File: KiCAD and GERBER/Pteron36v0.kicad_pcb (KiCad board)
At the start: 2 copper layers, 140.1 x 108.1 mm, 56 parts, among them J1 AudioJack4, J2 AudioJack4, J3 Conn_01x04, SW10 SW_PUSH, SW12 SW_PUSH, SW13 SW_PUSH, SW14 SW_PUSH, SW15 SW_PUSH, SW17 SW_PUSH, SW18 SW_PUSH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

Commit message: merge version 1.2.0 pcb into main
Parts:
- SW10, SW12, SW13, SW14, SW15, SW17, SW18, SW19, SW20, SW22, SW23, SW24, SW26, SW27, SW28, SW7, SW8, SW9: footprint Universal-Switch-Footprint:MX-ALPs-PG1350-FLIP -> Universal-Switch-Footprint:MX-ALPs-PG1350-FLIP-fix
- moved D10 12.7 mm to (114.8, 114.3), turned to 102.5 degrees
- moved D15 12.1 mm to (96.3, 123.1), turned to 115 degrees
- moved D20 11.1 mm to (80.8, 134.2), turned to 127.5 degrees
- moved D17 10.4 mm to (150.0, 52.3), turned to 90 degrees
- moved D12 10.3 mm to (170.1, 52.8), turned to 90 degrees
- moved D18 10.1 mm to (150.0, 69.0), turned to 90 degrees
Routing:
- net /Row3: track 193.1 -> 170.5 mm
- net Net-(D17-Pad2): track 20.6 -> 36.2 mm
- net /Col3: track 197.4 -> 182.6 mm, vias 3 -> 2
- net Net-(D15-Pad2): track 18.9 -> 33.3 mm
- net /Row1: track 227.9 -> 213.9 mm
- net Net-(D13-Pad2): track 21.7 -> 35.2 mm
- net Net-(D8-Pad2): track 17.6 -> 30.5 mm
- net Net-(D7-Pad2): track 20.4 -> 33.3 mm
- net Net-(D26-Pad2): track 17.4 -> 30.1 mm
- net Net-(D28-Pad2): track 21.9 -> 34.6 mm
- net Net-(D22-Pad2): track 22.8 -> 35.5 mm
- net Net-(D27-Pad2): track 23.9 -> 36.5 mm
- net /Row2: track 238.3 -> 225.8 mm, vias 4 -> 3
- net Net-(D9-Pad2): track 19.9 -> 32.1 mm
- net Net-(D18-Pad2): track 17.5 -> 29.8 mm
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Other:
- board text added: "Pteron36 V1.2.0"

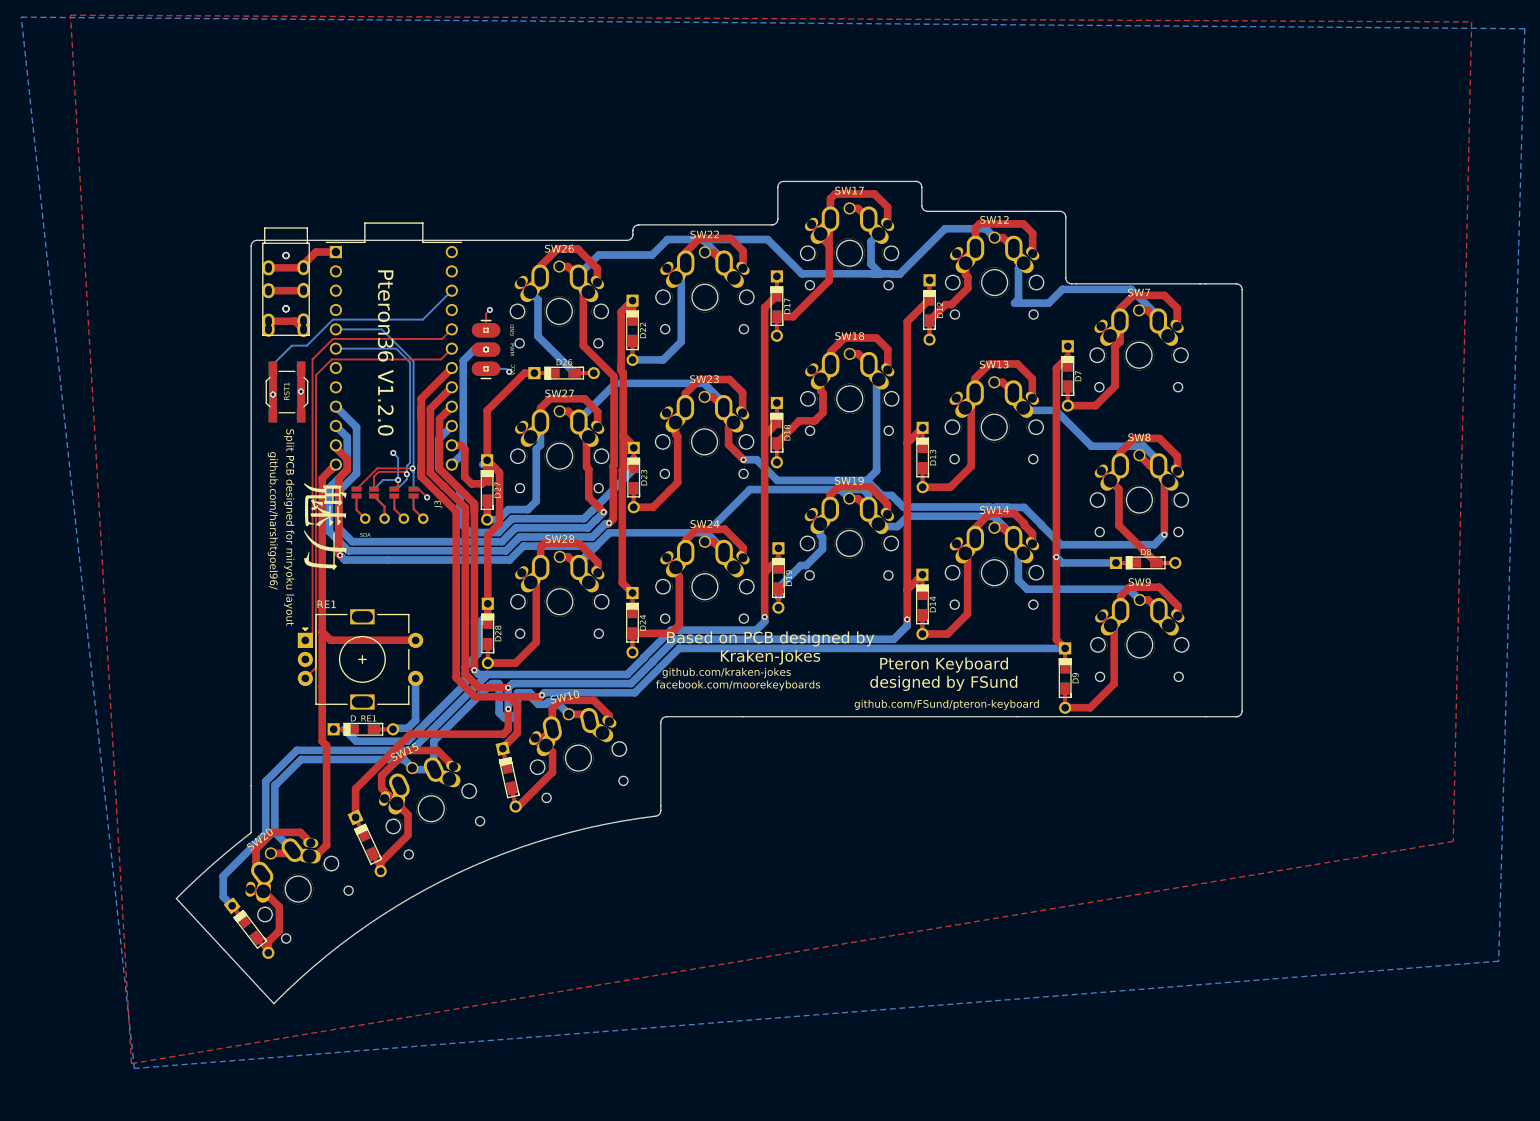
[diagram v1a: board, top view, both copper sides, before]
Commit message: use crkbd footprint for better manufacturing
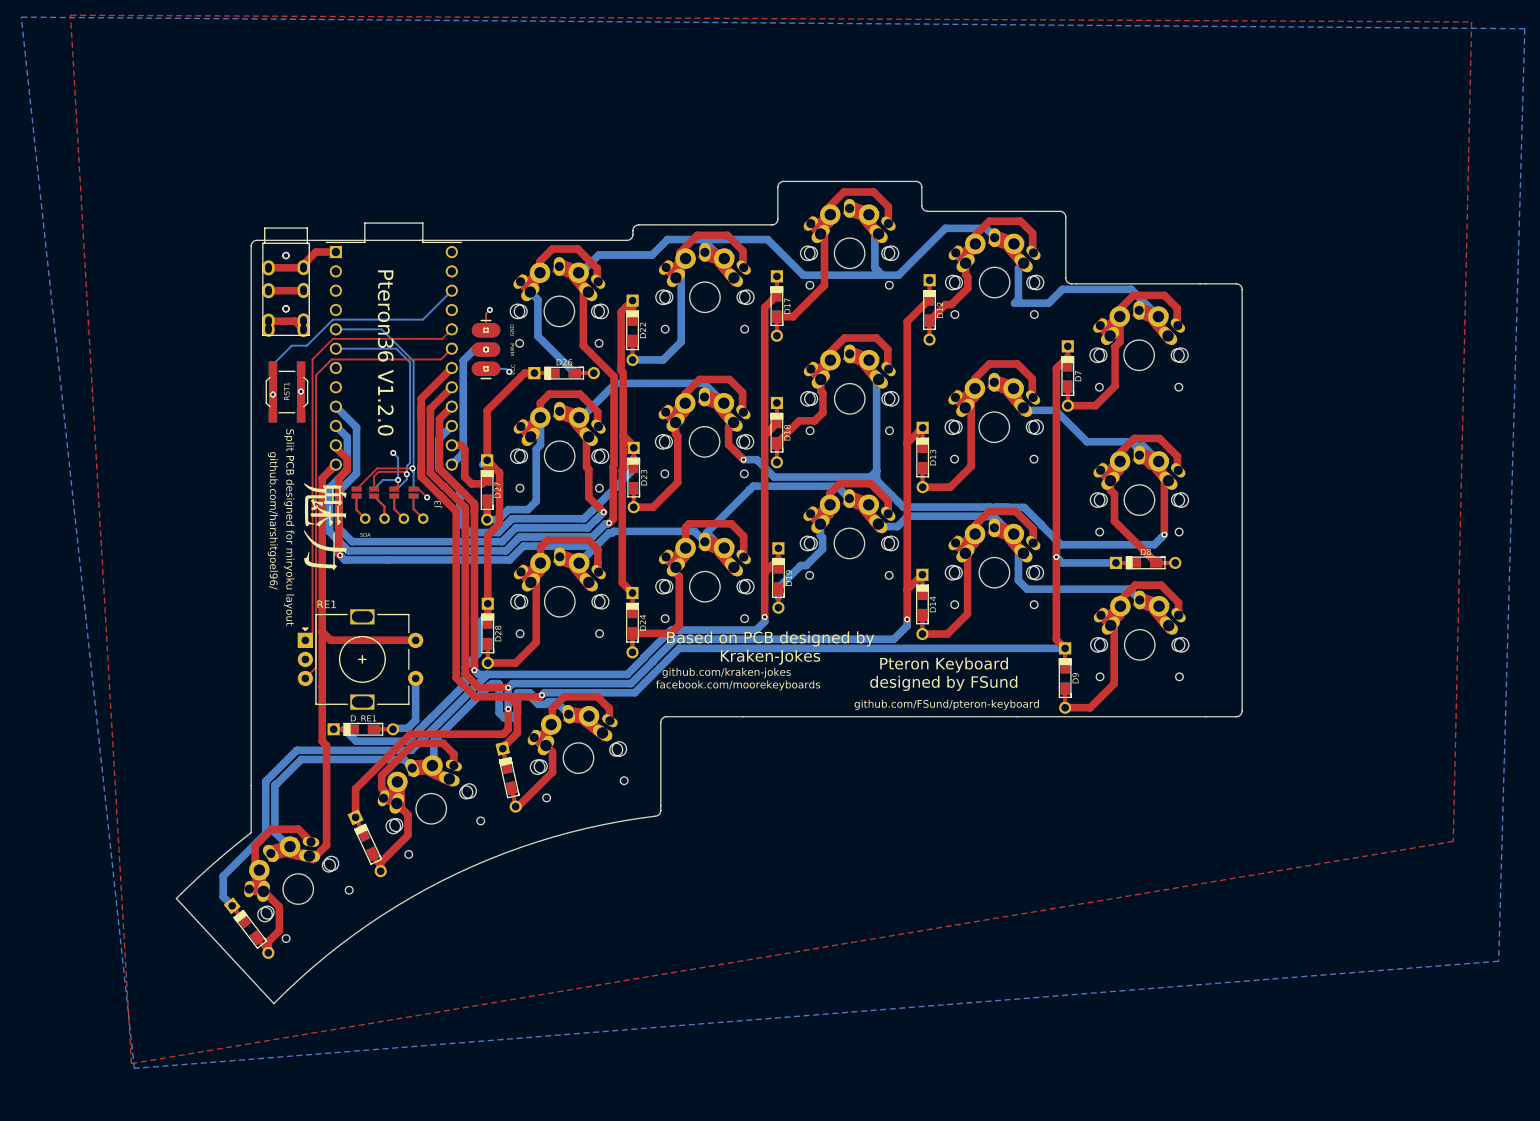
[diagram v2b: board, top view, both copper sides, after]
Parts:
- SW10, SW12, SW13, SW14, SW15, SW17, SW18, SW19, SW20, SW22, SW23, SW24, SW26, SW27, SW28, SW7, SW8, SW9: footprint Universal-Switch-Footprint:MX-ALPs-PG1350-FLIP-fix -> User-Submitted:uni-new
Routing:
- net /Row3: track 170.5 -> 165.1 mm
- net Net-(D24-Pad2): track 30.7 -> 34.2 mm
- net Net-(D22-Pad2): track 35.5 -> 38.2 mm
- net Net-(D17-Pad2): track 36.2 -> 34.0 mm
- net Net-(D27-Pad2): track 36.5 -> 38.7 mm
- net Net-(D19-Pad2): track 28.9 -> 30.9 mm
- net Net-(D15-Pad2): track 33.3 -> 35.0 mm
- net Net-(D28-Pad2): track 34.6 -> 36.0 mm
- net Net-(D26-Pad2): track 30.1 -> 31.4 mm
- net /Row2: track 225.8 -> 226.8 mm
- net Net-(D10-Pad2): track 27.8 -> 28.7 mm
- net /Row1: track 213.9 -> 213.0 mm
- net Net-(D12-Pad2): track 28.2 -> 27.3 mm
- net Net-(D9-Pad2): track 32.1 -> 32.8 mm

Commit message: update footprint for better support from manuf
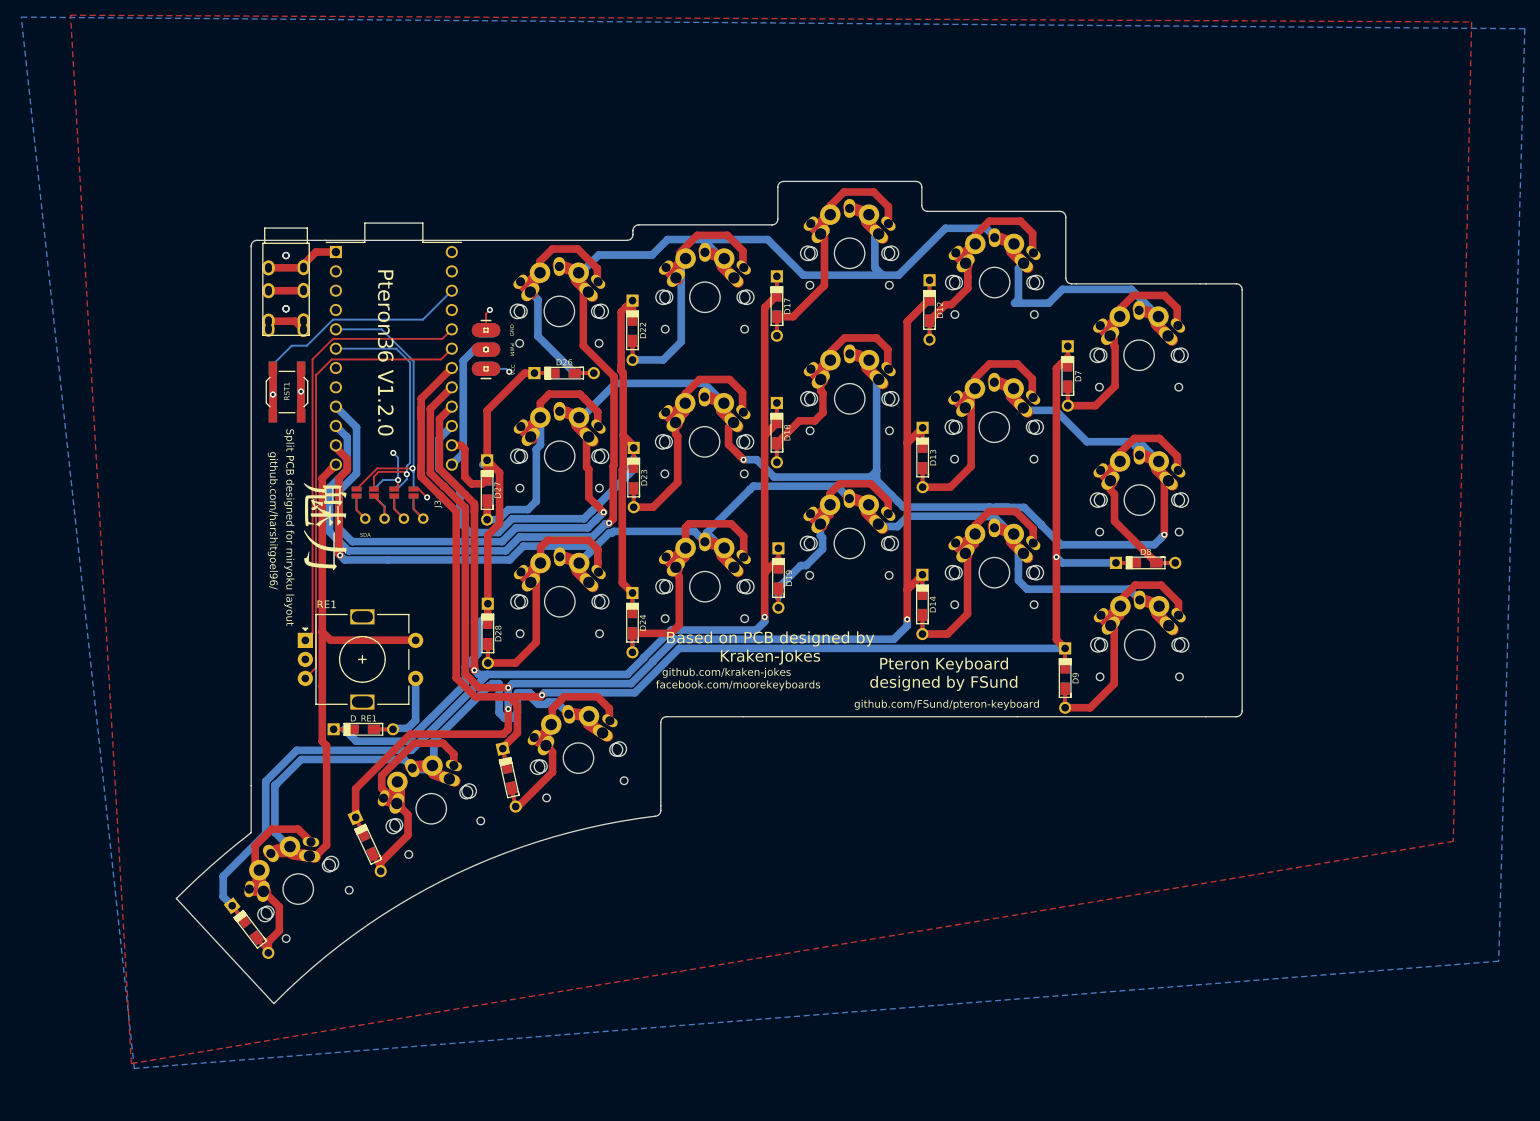
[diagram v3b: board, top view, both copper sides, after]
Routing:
- net /Row1: track 213.0 -> 192.3 mm
- net /Row2: track 226.8 -> 216.8 mm
- net Net-(D22-Pad2): track 38.2 -> 30.5 mm
- net Net-(D28-Pad2): track 36.0 -> 30.9 mm
- net Net-(D13-Pad2): track 35.2 -> 30.2 mm
- net Net-(D17-Pad2): track 34.0 -> 29.1 mm
- net /Row3: track 165.1 -> 160.2 mm
- net Net-(D7-Pad2): track 33.3 -> 28.6 mm
- net Net-(D12-Pad2): track 27.3 -> 23.0 mm
- net Net-(D8-Pad2): track 30.5 -> 26.2 mm
- net Net-(D26-Pad2): track 31.4 -> 29.6 mm

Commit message: reroute pcb, just for kicks
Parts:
- moved D8 13.1 mm to (188.2, 77.8), turned to 90 degrees
- moved D9 4.37 mm to (188.2, 96.9)
- moved JP1 1.17 mm to (103.4, 76.9)
- moved JP2 1.17 mm to (100.9, 76.9)
- moved JP5 1.17 mm to (103.4, 76.9)
- moved JP6 1.17 mm to (100.9, 76.9)
- moved JP3 1.17 mm to (98.2, 76.9)
- moved JP4 1.17 mm to (95.9, 76.9)
- moved JP7 1.17 mm to (98.2, 76.9)
- moved JP8 1.17 mm to (95.9, 76.9)
- moved D12 0.91 mm to (169.1, 52.9)
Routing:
- net /Row4: track 144.7 -> 307.5 mm
- net /Row2: track 216.8 -> 306.4 mm, vias 3 -> 4
- net /Row3: track 160.2 -> 243.4 mm
- net /Col2: track 185.4 -> 221.5 mm, vias 3 -> 0
- net /Col1: track 187.8 -> 218.6 mm, vias 2 -> 0
- net /Row1: track 192.3 -> 171.5 mm, vias 1 -> 0
- net /Col3: track 182.6 -> 197.5 mm, vias 2 -> 0
- net Net-(D15-Pad2): track 35.0 -> 20.9 mm
- net Net-(D9-Pad2): track 32.8 -> 22.7 mm
- net /Col4: track 86.2 -> 76.2 mm, vias 0 -> 1
- net Net-(D27-Pad2): track 38.7 -> 29.7 mm
- net Net-(D20-Pad2): track 26.5 -> 17.8 mm
- net VCC: track 16.7 -> 8.91 mm, vias 3 -> 2
- net Net-(D12-Pad2): track 23.0 -> 30.4 mm
- net GND: track 22.6 -> 15.5 mm
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
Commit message: final pcb
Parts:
- added H1: MountingHole, MountingHole:MountingHole_2.2mm_M2, F.Cu at (177.8, 106.3)
- added H2: MountingHole, MountingHole:MountingHole_2.2mm_M2, F.Cu at (177.8, 63.5)
- added H3: MountingHole, MountingHole:MountingHole_2.2mm_M2, F.Cu at (139.7, 106.3)
- added H4: MountingHole, MountingHole:MountingHole_2.2mm_M2, F.Cu at (101.5, 58.8)
- added H5: MountingHole, MountingHole:MountingHole_2.2mm_M2, F.Cu at (139.7, 65.5)
- added H6: MountingHole, MountingHole:MountingHole_2.2mm_M2, F.Cu at (86.6, 119.1)
- moved D9 4.95 mm to (187.4, 101.7)
- moved JP2 4.95 mm to (100.1, 81.8)
- moved JP6 4.95 mm to (100.1, 81.8)
- moved U1 4.95 mm to (98.8, 64.1)
- moved SW9 4.95 mm to (196.9, 101.7)
- moved D8 4.95 mm to (187.4, 82.7)
- moved SW8 4.95 mm to (196.8, 82.7)
- moved D14 4.95 mm to (168.3, 96.4)
- moved D20 4.95 mm to (80.0, 139.1)
- moved SW22 4.95 mm to (139.7, 56.0)
- moved JP3 4.95 mm to (97.4, 81.8)
- moved JP4 4.95 mm to (95.1, 81.8)
- moved JP7 4.95 mm to (97.4, 81.8)
- moved JP8 4.95 mm to (95.1, 81.8)
- moved SW19 4.95 mm to (158.7, 88.4)
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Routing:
- net /Row4: track 307.5 -> 292.0 mm
- net /Row3: track 243.4 -> 248.0 mm
- net /Row2: track 306.4 -> 302.5 mm
- net /Col1: track 218.6 -> 222.2 mm
- net Net-(D20-Pad2): track 17.8 -> 19.2 mm
- net /Col2: track 221.5 -> 220.2 mm
- net /Col3: track 197.5 -> 196.5 mm
- net Net-(D28-Pad2): track 29.7 -> 28.9 mm
- net Net-(D13-Pad2): vias 0 -> 2
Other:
- board text added: "Based on Pteron keyboard by Fsund Based on Pteron pcb by Kraken-Jokes"
- board text added: "Pteron36 V1.2.0b"
- board text removed: "Based on PCB designed by Kraken-Jokes"
- board text removed: "Pteron Keyboard designed by FSund"
- board text removed: "Pteron36 V1.2.0"
- board text removed: "facebook.com/moorekeyboards"
- board text removed: "github.com/FSund/pteron-keyboard"
- board text removed: "github.com/kraken-jokes"

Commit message: generate final gerber
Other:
- board text added: "Pteron36 V1.3.0"
- board text removed: "Pteron36 V1.2.0b"
